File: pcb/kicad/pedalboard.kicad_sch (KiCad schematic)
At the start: 0 parts

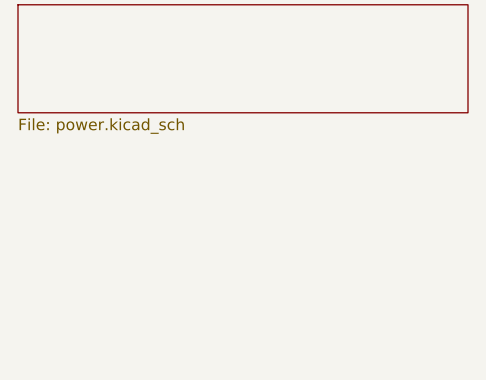
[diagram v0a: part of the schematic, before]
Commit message: Pedalboard PCB: Pi header and connectors sheet
The 40-pin socket (5 V, the 3.3 V enable, I2C1, I2S, HAT+ ID pins),
the HAT+ ID EEPROM (CAT24C32 at 0x50), the power button lead to the
Pi 5's J2 pads, screen power (PH2.0 socket or a 2-pin header), test
points and mounting holes. The schematic's UUIDs are now stable, so
regenerating it keeps the PCB's links to the symbols.

Co-Authored-By: Claude Opus 5.5 <noreply@anthropic.com>
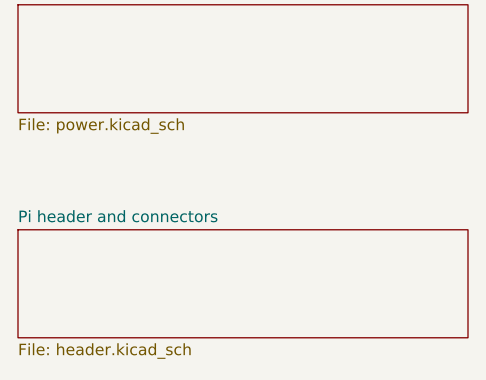
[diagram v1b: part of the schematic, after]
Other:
- added sheet Pi header and connectors (header.kicad_sch)
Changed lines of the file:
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@@
 		(instances
 			(project "pedalboard"
-				(path "/411c5051-cc08-4299-b424-2e3c8bc5a0e5"
+				(path "/3bcc4b79-1880-583a-b0ae-d715fcf404f8"
 					(page "2")
 				)
 			)
+		)
+	)
+	(sheet
+		(at 30 55)
+		(size 50 12)
+		(exclude_from_sim no)
+		(in_bom yes)
+		(on_board yes)
+		(dnp no)
+		(stroke
+			(width 0)
+			(type solid)
+		)
+		(fill
+			(color 0 0 0 0)
+		)
+		(property "Sheetname" "Pi header and connectors"
+			(at 30 54.3 0)
+			(effects
+				(font
+					(size 1.27 1.27)
+				)
+				(justify left bottom)
+			)
+		)
+		(property "Sheetfile" "header.kicad_sch"
+			(at 30 67.6 0)
+			(effects
+				(font
+					(size 1.27 1.27)
+				)
+				(justify left top)
+			)
+		)
+		(instances
+			(project "pedalboard"
+				(path "/3bcc4b79-1880-583a-b0ae-d715fcf404f8"
+					(page "3")
+				)
+			)

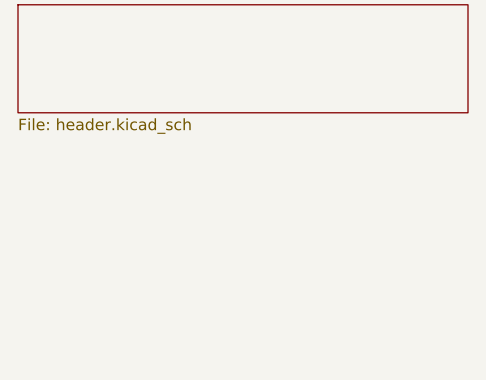
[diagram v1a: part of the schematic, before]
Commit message: Pedalboard PCB: audio converters and clocks sheet
PCM5122 DAC (0x4D, clock master) and PCM1863 ADC (0x4A), wired as the
HiFiBerry DAC+ADC Pro driver expects; Kyocera 22.5792 and 24.576 MHz
oscillators enabled by the DAC's GPIO6/GPIO3 and joined by an OR gate;
DAC output filters and the ADC's input filter from TI's datasheets.

Co-Authored-By: Claude Opus 5.5 <noreply@anthropic.com>
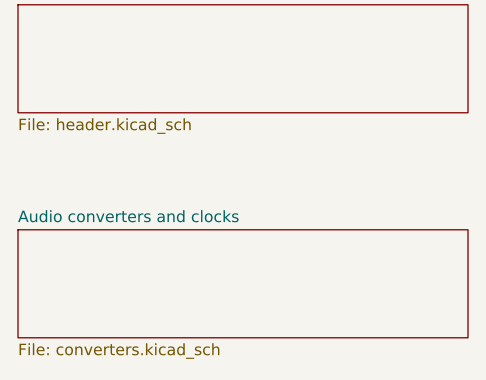
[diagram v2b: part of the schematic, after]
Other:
- added sheet Audio converters and clocks (converters.kicad_sch)
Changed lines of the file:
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@@
+		)
+	)
+	(sheet
+		(at 30 80)
+		(size 50 12)
+		(exclude_from_sim no)
+		(in_bom yes)
+		(on_board yes)
+		(dnp no)
+		(stroke
+			(width 0)
+			(type solid)
+		)
+		(fill
+			(color 0 0 0 0)
+		)
+		(property "Sheetname" "Audio converters and clocks"
+			(at 30 79.3 0)
+			(effects
+				(font
+					(size 1.27 1.27)
+				)
+				(justify left bottom)
+			)
+		)
+		(property "Sheetfile" "converters.kicad_sch"
+			(at 30 92.6 0)
+			(effects
+				(font
+					(size 1.27 1.27)
+				)
+				(justify left top)
+			)
+		)
+		(instances
+			(project "pedalboard"
+				(path "/3bcc4b79-1880-583a-b0ae-d715fcf404f8"
+					(page "4")
+				)
+			)
 		)
 	)

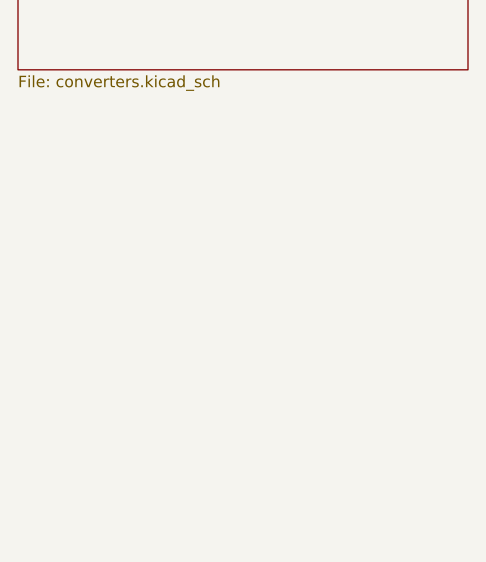
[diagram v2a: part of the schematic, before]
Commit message: Pedalboard PCB: guitar input and outputs sheets
Guitar input: 5 V reference, protected 1 Mohm input, OPA1642 gain
stage (0 to +24 dB), LM393 clip LED with a hold. Outputs: main volume,
OPA1642 buffers and impedance-balanced TRS jacks; headphone volume into
the TPA6130A2, with 10k ahead of the knob to keep its inputs in range.

Co-Authored-By: Claude Opus 5.5 <noreply@anthropic.com>
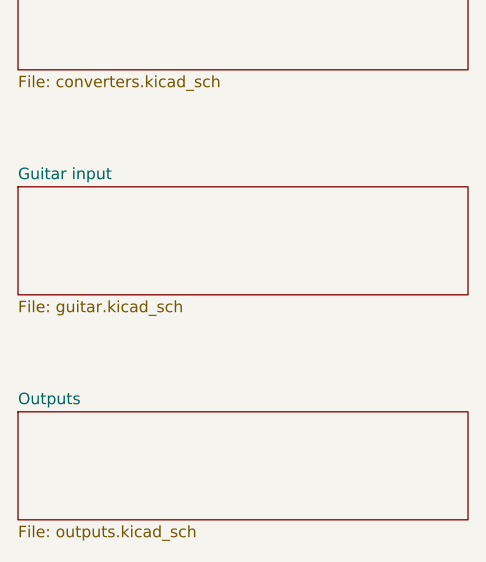
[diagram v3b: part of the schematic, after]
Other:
- added sheet Guitar input (guitar.kicad_sch)
- added sheet Outputs (outputs.kicad_sch)
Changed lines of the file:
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@@
+		)
+	)
+	(sheet
+		(at 30 105)
+		(size 50 12)
+		(exclude_from_sim no)
+		(in_bom yes)
+		(on_board yes)
+		(dnp no)
+		(stroke
+			(width 0)
+			(type solid)
+		)
+		(fill
+			(color 0 0 0 0)
+		)
+		(property "Sheetname" "Guitar input"
+			(at 30 104.3 0)
+			(effects
+				(font
+					(size 1.27 1.27)
+				)
+				(justify left bottom)
+			)
+		)
+		(property "Sheetfile" "guitar.kicad_sch"
+			(at 30 117.6 0)
+			(effects
+				(font
+					(size 1.27 1.27)
+				)
+				(justify left top)
+			)
+		)
+		(instances
+			(project "pedalboard"
+				(path "/3bcc4b79-1880-583a-b0ae-d715fcf404f8"
+					(page "5")
+				)
+			)
+		)
+	)
+	(sheet
+		(at 30 130)
+		(size 50 12)
+		(exclude_from_sim no)
+		(in_bom yes)
+		(on_board yes)
+		(dnp no)
+		(stroke
+			(width 0)
+			(type solid)
+		)
+		(fill
+			(color 0 0 0 0)
+		)
+		(property "Sheetname" "Outputs"
+			(at 30 129.3 0)
+			(effects
+				(font
+					(size 1.27 1.27)
+				)
+				(justify left bottom)
+			)
+		)
+		(property "Sheetfile" "outputs.kicad_sch"
+			(at 30 142.6 0)
+			(effects
+				(font
+					(size 1.27 1.27)
+				)
+				(justify left top)
+			)
+		)
+		(instances
+			(project "pedalboard"
+				(path "/3bcc4b79-1880-583a-b0ae-d715fcf404f8"
+					(page "6")
+				)
+			)
 		)
 	)

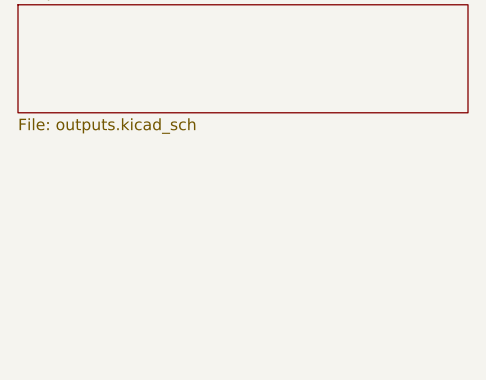
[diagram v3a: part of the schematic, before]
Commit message: Pedalboard PCB: footswitch controller sheet
A socketed Raspberry Pi Pico reads 8 footswitches and drives 8 LEDs
over 4-pin JST-XH leads, with ESD arrays at the connectors; expression
pedal input with tip/ring swap jumpers; MIDI out on 3.5 mm TRS Type A
with the MIDI 3.3 V values. Completes the schematic.

Co-Authored-By: Claude Opus 5.5 <noreply@anthropic.com>
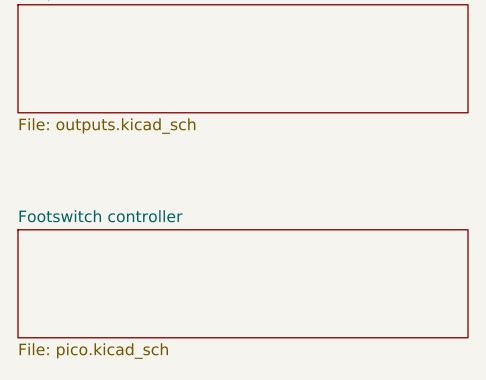
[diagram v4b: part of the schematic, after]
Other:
- added sheet Footswitch controller (pico.kicad_sch)
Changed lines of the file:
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@@
+		)
+	)
+	(sheet
+		(at 30 155)
+		(size 50 12)
+		(exclude_from_sim no)
+		(in_bom yes)
+		(on_board yes)
+		(dnp no)
+		(stroke
+			(width 0)
+			(type solid)
+		)
+		(fill
+			(color 0 0 0 0)
+		)
+		(property "Sheetname" "Footswitch controller"
+			(at 30 154.3 0)
+			(effects
+				(font
+					(size 1.27 1.27)
+				)
+				(justify left bottom)
+			)
+		)
+		(property "Sheetfile" "pico.kicad_sch"
+			(at 30 167.6 0)
+			(effects
+				(font
+					(size 1.27 1.27)
+				)
+				(justify left top)
+			)
+		)
+		(instances
+			(project "pedalboard"
+				(path "/3bcc4b79-1880-583a-b0ae-d715fcf404f8"
+					(page "7")
+				)
+			)
 		)
 	)
